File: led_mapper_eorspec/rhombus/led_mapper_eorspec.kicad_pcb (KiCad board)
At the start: 4 copper layers, 116 x 67 mm, 2117 parts, among them J1 Conn_02x12_Top_Bottom

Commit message: Complete single-net schematic, led placement and vertical tracks
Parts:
- removed D1000, D1001, D1002, D1003, D1004, D1005, D1006, D1007, D1008, D1009, D1010, D1011, D1012, D1013, D1014, D1015, D1016, D1017, D1018, D1019, D1020, D1021, D1022, D1023, D1024, D1025, D1026, D1027, D1028, D1029, D1030, D1031, D1032, D1033, D1034, D1035, D1036, D1037, D1038, D1039, D1040, D1041, D1042, D1043, D1044, D1045, D1046, D1047, D1048, D1049, D1050, D1051, D1052, D1053, D1054, D1055, D1056, D1057, D1058, D1059, D1060, D1061, D1062, D1063, D1064, D1065, D1066, D1067, D1068, D1069, D1070, D1071, D1072, D1073, D1074, D1075, D1076, D1077, D1078, D1079, D1080, D1081, D1082, D1083, D1084, D1085, D1086, D1087, D1088, D1089, D1090, D1091, D1092, D1093, D1094, D1095, D1096, D1097, D1098, D1099, D1100, D1101, D1102, D1103, D1104, D1105, D1106, D1107, D1108, D1109, D1110, D1111, D1112, D1113, D1114, D1115, D1116, D1117, D1118, D1119, D1120, D1121, D1122, D1123, D1124, D1125, D1126, D1127, D1128, D1129, D1130, D1131, D1132, D1133, D1134, D1135, D1136, D1137, D1138, D1139, D1140, D1141, D1142, D1143, D1144, D1145, D1146, D1147, D1148, D1149, D1150, D1151, D1152, D1153, D1154, D1155, D1156, D1157, D1158, D1159, D1160, D1161, D1162, D1163, D1164, D1165, D1166, D1167, D1168, D1169, D1170, D1171, D1172, D1173, D1174, D1175, D1176, D1177, D1178, D1179, D1180, D1181, D1182, D1183, D1184, D1185, D1186, D1187, D1188, D1189, D1190, D1191, D1192, D1193, D1194, D1195, D1196, D1197, D1198, D1199, D1200, D1201, D1202, D1203, D1204, D1205, D1206, D1207, D1208, D1209, D1210, D1211, D1212, D1213, D1214, D1215, D1216, D1217, D1218, D1219, D1220, D1221, D1222, D1223, D1224, D1225, D1226, D1227, D1228, D1229, D1230, D1231, D1232, D1233, D1234, D1235, D1236, D1237, D1238, D1239, D1240, D1241, D1242, D1243, D1244, D1245, D1246, D1247, D1248, D1249, D1250, D1251, D1252, D1253, D1254, D1255, D1256, D1257, D1258, D1259, D1260, D1261, D1262, D1263, D1264, D1265, D1266, D1267, D1268, D1269, D1270, D1271, D1272, D1273, D1274, D1275, D1276, D1277, D1278, D1279, D1280, D1281, D1282, D1283, D1284, D1285, D1286, D1287, D1288, D1289, D1290, D1291, D1292, D1293, D1294, D1295, D1296, D1297, D1298, D1299, D1300, D1301, D1302, D1303, D1304, D1305, D1306, D1307, D1308, D1309, D1310, D1311, D1312, D1313, D1314, D1315, D1316, D1317, D1318, D1319, D1320, D1321, D1322, D1323, D1324, D1325, D1326, D1327, D1328, D1329, D1330, D1331, D1332, D1333, D1334, D1335, D1336, D1337, D1338, D1339, D1340, D1341, D1342, D1343, D1344, D1345, D1346, D1347, D1348, D1349, D1350, D1351, D1352, D1353, D1354, D1355, D1356, D1357, D1358, D1359, D1360, D1361, D1362, D1363, D1364, D1365, D1366, D1367, D1368, D1369, D1370, D1371, D1372, D1373, D1374, D1375, D1376, D1377, D1378, D1379, D1380, D1381, D1382, D1383, D1384, D1385, D1386, D1387, D1388, D1389, D1390, D1391, D1392, D1393, D1394, D1395, D1396, D1397, D1398, D1399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: LED, ccatlib:LED_0201_0603Metric_XINGLIGHT
- D1, D10, D100, D101, D102, D103, D104, D105, D106, D107, D108, D109, D11, D110, D111, D112, D113, D114, D115, D116, D117, D118, D119, D12, D120, D121, D122, D123, D124, D125, D126, D127, D128, D129, D13, D130, D131, D132, D133, D134, D135, D136, D137, D138, D139, D14, D140, D141, D142, D143, D144, D145, D146, D147, D148, D149, D15, D150, D151, D152, D153, D154, D155, D156, D157, D158, D159, D16, D160, D161, D162, D163, D164, D165, D166, D167, D168, D169, D17, D170, D171, D172, D173, D174, D175, D176, D177, D178, D179, D18, D180, D181, D182, D183, D184, D185, D186, D187, D188, D189, D19, D190, D191, D192, D193, D194, D195, D196, D197, D198, D199, D2, D20, D200, D201, D202, D203, D204, D205, D206, D207, D208, D209, D21, D210, D211, D212, D213, D214, D215, D216, D217, D218, D219, D22, D220, D221, D222, D223, D224, D225, D226, D227, D228, D229, D23, D230, D231, D232, D233, D234, D235, D236, D237, D238, D239, D24, D240, D241, D242, D243, D244, D245, D246, D247, D248, D249, D25, D250, D251, D252, D253, D254, D255, D256, D257, D258, D259, D26, D260, D261, D262, D263, D264, D265, D266, D267, D268, D269, D27, D270, D271, D272, D273, D274, D275, D276, D277, D278, D279, D28, D280, D281, D282, D283, D284, D285, D286, D287, D288, D289, D29, D290, D291, D292, D293, D294, D295, D296, D297, D298, D299, D3, D30, D300, D301, D302, D303, D304, D305, D306, D307, D308, D309, D31, D310, D311, D312, D313, D314, D315, D316, D317, D318, D319, D32, D320, D321, D322, D323, D324, D325, D326, D327, D328, D329, D33, D330, D331, D332, D333, D334, D335, D336, D337, D338, D339, D34, D340, D341, D342, D343, D344, D345, D346, D347, D348, D349, D35, D350, D351, D352, D353, D354, D355, D356, D357, D358, D359, D36, D360, D361, D362, D363, D364, D365, D366, D367, D368, D369, D37, D370, D371, D372, D373, D374, D375, D376, D377, D378, D379, D38, D380, D381, D382, D383, D384, D385, D386, D387, D388, D389, D39, D390, D391, D392, D393, D394, D395, D396, D397, D398, D399, D4, D40, D400, D401, D402, D403, D404, D405, D406, D407, D408, D409, D41, D410, D411, D412, D413, D414, D415, D416, D417, D418, D419, D42, D420, D421, D422, D423, D424, D425, D426, D427, D428, D429, D43, D430, D431, D432, D433, D434, D435, D436, D437, D438, D439, D44, D440, D441, D442, D443, D444, D445, D446, D447, D448, D449, D45, D450, D451, D452, D453, D454, D455, D456, D457, D458, D459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: value LED -> LED_45deg; footprint ccatlib:LED_0201_0603Metric_XINGLIGHT -> LED_SMD:LED_0201_0603Metric
- moved J1 203.9 mm to (246.4, 90.7)
- moved D96 93.7 mm to (94.4, 22.5), turned to 180 degrees
- moved D416 93.6 mm to (83.9, 40.6), turned to 180 degrees
- moved D95 93.1 mm to (92.3, 22.5), turned to 180 degrees
- moved D415 93.0 mm to (81.8, 40.6), turned to 180 degrees
- moved D94 92.4 mm to (90.2, 22.5), turned to 180 degrees
- moved D93 91.7 mm to (88.1, 22.5), turned to 180 degrees
- moved D512 87.8 mm to (80.8, 46.0), turned to 180 degrees
- moved D192 87.3 mm to (91.2, 27.9), turned to 180 degrees
- moved D511 87.2 mm to (78.7, 46.0), turned to 180 degrees
- moved D191 86.7 mm to (89.2, 27.9), turned to 180 degrees
- moved D510 86.5 mm to (76.6, 46.0), turned to 180 degrees
- moved D190 86.0 mm to (87.1, 27.9), turned to 180 degrees
- moved D509 85.9 mm to (74.5, 46.0), turned to 180 degrees
- moved D189 85.3 mm to (85.0, 27.9), turned to 180 degrees
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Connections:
- D100 pad 1: /P22 -> /P21
- D100 pad 2: /P8 -> /P4
- D101 pad 1: /P22 -> /P21
- D101 pad 2: /P9 -> /P5
- D102 pad 1: /P22 -> /P21
- D102 pad 2: /P10 -> /P6
- D103 pad 1: /P22 -> /P21
- D103 pad 2: /P11 -> /P7
- D104 pad 1: /P22 -> /P21
- D104 pad 2: /P12 -> /P8
- D105 pad 1: /P22 -> /P21
- D105 pad 2: /P13 -> /P9
- D106 pad 1: /P22 -> /P21
- D106 pad 2: /P14 -> /P10
- D107 pad 1: /P22 -> /P21
- D107 pad 2: /P15 -> /P11
- D108 pad 1: /P22 -> /P21
- D108 pad 2: /P16 -> /P12
- D109 pad 1: /P22 -> /P21
- D109 pad 2: /P17 -> /P13
- D110 pad 1: /P22 -> /P21
- D110 pad 2: /P18 -> /P14
- D111 pad 1: /P22 -> /P21
- D111 pad 2: /P19 -> /P15
- D112 pad 1: /P22 -> /P21
- D112 pad 2: /P20 -> /P16
- D113 pad 1: /P22 -> /P21
- D113 pad 2: /P21 -> /P17
- D114 pad 1: /P22 -> /P21
- D114 pad 2: /P23 -> /P18
- D115 pad 1: /P22 -> /P21
- D115 pad 2: /P24 -> /P19
- D116 pad 1: /P10 -> /P21
- D116 pad 2: /P1 -> /P20
- D117 pad 1: /P10 -> /P21
- D117 pad 2: /P2 -> /P22
- D118 pad 1: /P10 -> /P21
- D118 pad 2: /P3 -> /P23
- D119 pad 1: /P10 -> /P21
- D119 pad 2: /P4 -> /P24
- D120 pad 1: /P10 -> /P5
- D120 pad 2: /P5 -> /P1
- D121 pad 1: /P10 -> /P5
- D121 pad 2: /P6 -> /P2
- D122 pad 1: /P10 -> /P5
- D122 pad 2: /P7 -> /P3
- D123 pad 1: /P10 -> /P5
- D123 pad 2: /P8 -> /P4
- D124 pad 1: /P10 -> /P5
- D124 pad 2: /P9 -> /P6
- D125 pad 1: /P10 -> /P5
- D125 pad 2: /P11 -> /P7
- D126 pad 1: /P10 -> /P5
- D126 pad 2: /P12 -> /P8
- D127 pad 1: /P10 -> /P5
- D127 pad 2: /P13 -> /P9
- D128 pad 1: /P10 -> /P5
- D128 pad 2: /P14 -> /P10
- D129 pad 1: /P10 -> /P20
- D129 pad 2: /P15 -> /P1
- D130 pad 1: /P10 -> /P20
- D130 pad 2: /P16 -> /P2
- D131 pad 1: /P10 -> /P20
- D131 pad 2: /P17 -> /P3
- D132 pad 1: /P10 -> /P20
- D132 pad 2: /P18 -> /P4
- D133 pad 1: /P10 -> /P20
- D133 pad 2: /P19 -> /P5
- D134 pad 1: /P10 -> /P20
- D134 pad 2: /P20 -> /P6
- D135 pad 1: /P10 -> /P20
- D135 pad 2: /P21 -> /P7
- D136 pad 1: /P10 -> /P20
- D136 pad 2: /P22 -> /P8
- D137 pad 1: /P10 -> /P20
- D137 pad 2: /P23 -> /P9
- D138 pad 1: /P10 -> /P20
- D138 pad 2: /P24 -> /P10
- D139 pad 1: /P21 -> /P20
- D139 pad 2: /P1 -> /P11
- D140 pad 1: /P21 -> /P20
- D140 pad 2: /P2 -> /P12
- D141 pad 1: /P21 -> /P20
- D141 pad 2: /P3 -> /P13
- D142 pad 1: /P21 -> /P20
- D142 pad 2: /P4 -> /P14
- D143 pad 1: /P21 -> /P20
- D143 pad 2: /P5 -> /P15
- D144 pad 1: /P21 -> /P20
- D144 pad 2: /P6 -> /P16
- D145 pad 1: /P21 -> /P20
- D145 pad 2: /P7 -> /P17
- D146 pad 1: /P21 -> /P20
- D146 pad 2: /P8 -> /P18
- D147 pad 1: /P21 -> /P20
- D147 pad 2: /P9 -> /P19
- D148 pad 1: /P21 -> /P20
- D148 pad 2: /P10 -> /P21
- D149 pad 1: /P21 -> /P20
- D149 pad 2: /P11 -> /P22
- D150 pad 1: /P21 -> /P20
- D150 pad 2: /P12 -> /P23
- D151 pad 1: /P21 -> /P20
- D151 pad 2: /P13 -> /P24
- D152 pad 1: /P21 -> /P4
- D152 pad 2: /P14 -> /P1
- D153 pad 1: /P21 -> /P4
- D153 pad 2: /P15 -> /P2
- D154 pad 1: /P21 -> /P4
- D154 pad 2: /P16 -> /P3
- D155 pad 1: /P21 -> /P4
- D155 pad 2: /P17 -> /P5
- D156 pad 1: /P21 -> /P4
- D156 pad 2: /P18 -> /P6
- D157 pad 1: /P21 -> /P4
- D157 pad 2: /P19 -> /P7
- D158 pad 1: /P21 -> /P4
- D158 pad 2: /P20 -> /P8
- D159 pad 1: /P21 -> /P4
- D159 pad 2: /P22 -> /P9
- D160 pad 1: /P21 -> /P4
- D160 pad 2: /P23 -> /P10
- D161 pad 1: /P21 -> /P19
- D161 pad 2: /P24 -> /P1
- D162 pad 1: /P9 -> /P19
- D162 pad 2: /P1 -> /P2
- D163 pad 1: /P9 -> /P19
- D163 pad 2: /P2 -> /P3
- D164 pad 1: /P9 -> /P19
- D164 pad 2: /P3 -> /P4
- D165 pad 1: /P9 -> /P19
- D165 pad 2: /P4 -> /P5
- D166 pad 1: /P9 -> /P19
- D166 pad 2: /P5 -> /P6
- D167 pad 1: /P9 -> /P19
- D167 pad 2: /P6 -> /P7
- D168 pad 1: /P9 -> /P19
- D168 pad 2: /P7 -> /P8
- D169 pad 1: /P9 -> /P19
- D169 pad 2: /P8 -> /P9
- D170 pad 1: /P9 -> /P19
- D171 pad 1: /P9 -> /P19
- D172 pad 1: /P9 -> /P19
- D173 pad 1: /P9 -> /P19
- D174 pad 1: /P9 -> /P19
- D175 pad 1: /P9 -> /P19
- D176 pad 1: /P9 -> /P19
- D177 pad 1: /P9 -> /P19
- D178 pad 1: /P9 -> /P19
- D179 pad 1: /P9 -> /P19
- D179 pad 2: /P19 -> /P20
- D180 pad 1: /P9 -> /P19
- D180 pad 2: /P20 -> /P21
- D181 pad 1: /P9 -> /P19
- D181 pad 2: /P21 -> /P22
- D182 pad 1: /P9 -> /P19
- D182 pad 2: /P22 -> /P23
- D183 pad 1: /P9 -> /P19
- D183 pad 2: /P23 -> /P24
- D184 pad 1: /P9 -> /P3
- D184 pad 2: /P24 -> /P1
- D185 pad 1: /P20 -> /P3
- D185 pad 2: /P1 -> /P2
- D186 pad 1: /P20 -> /P3
- D186 pad 2: /P2 -> /P4
- D187 pad 1: /P20 -> /P3
- D187 pad 2: /P3 -> /P5
- D188 pad 1: /P20 -> /P3
- D188 pad 2: /P4 -> /P6
- D189 pad 1: /P20 -> /P3
- D189 pad 2: /P5 -> /P7
- D190 pad 1: /P20 -> /P3
- D190 pad 2: /P6 -> /P8
- D191 pad 1: /P20 -> /P3
- D191 pad 2: /P7 -> /P9
- D192 pad 1: /P20 -> /P3
- D192 pad 2: /P8 -> /P10
- D193 pad 1: /P20 -> /P18
- D193 pad 2: /P9 -> /P1
- D194 pad 1: /P20 -> /P18
- D194 pad 2: /P10 -> /P2
- D195 pad 1: /P20 -> /P18
- D195 pad 2: /P11 -> /P3
- D196 pad 1: /P20 -> /P18
- D196 pad 2: /P12 -> /P4
- D197 pad 1: /P20 -> /P18
- D197 pad 2: /P13 -> /P5
- D198 pad 1: /P20 -> /P18
- D198 pad 2: /P14 -> /P6
- D199 pad 1: /P20 -> /P18
- D199 pad 2: /P15 -> /P7
- D200 pad 1: /P20 -> /P18
- D200 pad 2: /P16 -> /P8
- D201 pad 1: /P20 -> /P18
- D201 pad 2: /P17 -> /P9
- D202 pad 1: /P20 -> /P18
- D202 pad 2: /P18 -> /P10
- D203 pad 1: /P20 -> /P18
- D203 pad 2: /P19 -> /P11
- D204 pad 1: /P20 -> /P18
- D204 pad 2: /P21 -> /P12
- D205 pad 1: /P20 -> /P18
- D205 pad 2: /P22 -> /P13
- D206 pad 1: /P20 -> /P18
- D206 pad 2: /P23 -> /P14
- D207 pad 1: /P20 -> /P18
- D207 pad 2: /P24 -> /P15
- D208 pad 1: /P8 -> /P18
- D208 pad 2: /P1 -> /P16
- D209 pad 1: /P8 -> /P18
- D209 pad 2: /P2 -> /P17
- D210 pad 1: /P8 -> /P18
- D210 pad 2: /P3 -> /P19
- D211 pad 1: /P8 -> /P18
- D211 pad 2: /P4 -> /P20
- D212 pad 1: /P8 -> /P18
- D212 pad 2: /P5 -> /P21
- D213 pad 1: /P8 -> /P18
- D213 pad 2: /P6 -> /P22
- D214 pad 1: /P8 -> /P18
- D214 pad 2: /P7 -> /P23
- D215 pad 1: /P8 -> /P18
- D215 pad 2: /P9 -> /P24
- D216 pad 1: /P8 -> /P2
- D216 pad 2: /P10 -> /P1
- D217 pad 1: /P8 -> /P2
- D217 pad 2: /P11 -> /P3
- D218 pad 1: /P8 -> /P2
- D218 pad 2: /P12 -> /P4
- D219 pad 1: /P8 -> /P2
- D219 pad 2: /P13 -> /P5
- D220 pad 1: /P8 -> /P2
- D220 pad 2: /P14 -> /P6
- D221 pad 1: /P8 -> /P2
- D221 pad 2: /P15 -> /P7
- D222 pad 1: /P8 -> /P2
- D222 pad 2: /P16 -> /P8
- D223 pad 1: /P8 -> /P2
- D223 pad 2: /P17 -> /P9
- D224 pad 1: /P8 -> /P2
- D224 pad 2: /P18 -> /P10
- D225 pad 1: /P8 -> /P17
- D225 pad 2: /P19 -> /P1
- D226 pad 1: /P8 -> /P17
- D226 pad 2: /P20 -> /P2
- D227 pad 1: /P8 -> /P17
- D227 pad 2: /P21 -> /P3
- D228 pad 1: /P8 -> /P17
- D228 pad 2: /P22 -> /P4
- D229 pad 1: /P8 -> /P17
- D229 pad 2: /P23 -> /P5
- D230 pad 1: /P8 -> /P17
- D230 pad 2: /P24 -> /P6
- D231 pad 1: /P19 -> /P17
- D231 pad 2: /P1 -> /P7
- D232 pad 1: /P19 -> /P17
- D232 pad 2: /P2 -> /P8
- D233 pad 1: /P19 -> /P17
- D233 pad 2: /P3 -> /P9
- D234 pad 1: /P19 -> /P17
- D234 pad 2: /P4 -> /P10
- D235 pad 1: /P19 -> /P17
- D235 pad 2: /P5 -> /P11
- D236 pad 1: /P19 -> /P17
- D236 pad 2: /P6 -> /P12
- D237 pad 1: /P19 -> /P17
- D237 pad 2: /P7 -> /P13
- D238 pad 1: /P19 -> /P17
- D238 pad 2: /P8 -> /P14
- D239 pad 1: /P19 -> /P17
- D239 pad 2: /P9 -> /P15
- D24 pad 1: /P12 -> /P8
- D240 pad 1: /P19 -> /P17
- D240 pad 2: /P10 -> /P16
- D241 pad 1: /P19 -> /P17
- D241 pad 2: /P11 -> /P18
- D242 pad 1: /P19 -> /P17
- D242 pad 2: /P12 -> /P19
- D243 pad 1: /P19 -> /P17
- D243 pad 2: /P13 -> /P20
- D244 pad 1: /P19 -> /P17
- D244 pad 2: /P14 -> /P21
- D245 pad 1: /P19 -> /P17
- D245 pad 2: /P15 -> /P22
- D246 pad 1: /P19 -> /P17
- D246 pad 2: /P16 -> /P23
- D247 pad 1: /P19 -> /P17
- D247 pad 2: /P17 -> /P24
- D248 pad 1: /P19 -> /P1
- D248 pad 2: /P18 -> /P2
- D249 pad 1: /P19 -> /P1
- D249 pad 2: /P20 -> /P3
- D25 pad 1: /P12 -> /P8
- D250 pad 1: /P19 -> /P1
- D250 pad 2: /P21 -> /P4
- D251 pad 1: /P19 -> /P1
- D251 pad 2: /P22 -> /P5
- D252 pad 1: /P19 -> /P1
- D252 pad 2: /P23 -> /P6
- D253 pad 1: /P19 -> /P1
- D253 pad 2: /P24 -> /P7
- D254 pad 1: /P7 -> /P1
- D254 pad 2: /P1 -> /P8
- D255 pad 1: /P7 -> /P1
- D255 pad 2: /P2 -> /P9
- D256 pad 1: /P7 -> /P1
- D256 pad 2: /P3 -> /P10
- D257 pad 1: /P7 -> /P16
- D257 pad 2: /P4 -> /P1
- D258 pad 1: /P7 -> /P16
- D258 pad 2: /P5 -> /P2
- D259 pad 1: /P7 -> /P16
- D259 pad 2: /P6 -> /P3
- D26 pad 1: /P12 -> /P8
- D260 pad 1: /P7 -> /P16
- D260 pad 2: /P8 -> /P4
- D261 pad 1: /P7 -> /P16
- D261 pad 2: /P9 -> /P5
- D262 pad 1: /P7 -> /P16
- D262 pad 2: /P10 -> /P6
- D263 pad 1: /P7 -> /P16
- D263 pad 2: /P11 -> /P7
- D264 pad 1: /P7 -> /P16
- D264 pad 2: /P12 -> /P8
- D265 pad 1: /P7 -> /P16
- D265 pad 2: /P13 -> /P9
- D266 pad 1: /P7 -> /P16
- D266 pad 2: /P14 -> /P10
- D267 pad 1: /P7 -> /P16
- D267 pad 2: /P15 -> /P11
- D268 pad 1: /P7 -> /P16
- D268 pad 2: /P16 -> /P12
- D269 pad 1: /P7 -> /P16
- D269 pad 2: /P17 -> /P13
- D27 pad 1: /P12 -> /P8
- D270 pad 1: /P7 -> /P16
- D270 pad 2: /P18 -> /P14
- D271 pad 1: /P7 -> /P16
- D271 pad 2: /P19 -> /P15
- D272 pad 1: /P7 -> /P16
- D272 pad 2: /P20 -> /P17
- D273 pad 1: /P7 -> /P16
- D273 pad 2: /P21 -> /P18
- D274 pad 1: /P7 -> /P16
- D274 pad 2: /P22 -> /P19
- D275 pad 1: /P7 -> /P16
- D275 pad 2: /P23 -> /P20
- D276 pad 1: /P7 -> /P16
- D276 pad 2: /P24 -> /P21
- D277 pad 1: /P18 -> /P16
- D277 pad 2: /P1 -> /P22
- D278 pad 1: /P18 -> /P16
- D278 pad 2: /P2 -> /P23
- D279 pad 1: /P18 -> /P16
- D279 pad 2: /P3 -> /P24
- D28 pad 1: /P12 -> /P8
- D280 pad 1: /P18 -> /P8
- D280 pad 2: /P4 -> /P11
- D281 pad 1: /P18 -> /P8
- D281 pad 2: /P5 -> /P12
- D282 pad 1: /P18 -> /P8
- D282 pad 2: /P6 -> /P13
- D283 pad 1: /P18 -> /P8
- D283 pad 2: /P7 -> /P14
- D284 pad 1: /P18 -> /P8
- D284 pad 2: /P8 -> /P15
- D285 pad 1: /P18 -> /P8
- D285 pad 2: /P9 -> /P16
- D286 pad 1: /P18 -> /P8
- D286 pad 2: /P10 -> /P17
- D287 pad 1: /P18 -> /P8
- D287 pad 2: /P11 -> /P18
- D288 pad 1: /P18 -> /P8
- D288 pad 2: /P12 -> /P19
- D289 pad 1: /P18 -> /P15
- D289 pad 2: /P13 -> /P1
- D29 pad 1: /P12 -> /P8
- D290 pad 1: /P18 -> /P15
- D290 pad 2: /P14 -> /P2
- D291 pad 1: /P18 -> /P15
- D291 pad 2: /P15 -> /P3
- D292 pad 1: /P18 -> /P15
- D292 pad 2: /P16 -> /P4
- D293 pad 1: /P18 -> /P15
- D293 pad 2: /P17 -> /P5
- D294 pad 1: /P18 -> /P15
- D294 pad 2: /P19 -> /P6
- D295 pad 1: /P18 -> /P15
- D295 pad 2: /P20 -> /P7
- D296 pad 1: /P18 -> /P15
- D296 pad 2: /P21 -> /P8
- D297 pad 1: /P18 -> /P15
- D297 pad 2: /P22 -> /P9
- D298 pad 1: /P18 -> /P15
- D298 pad 2: /P23 -> /P10
- D299 pad 1: /P18 -> /P15
- D299 pad 2: /P24 -> /P11
- D30 pad 1: /P12 -> /P8
- D300 pad 1: /P6 -> /P15
- D300 pad 2: /P1 -> /P12
- D301 pad 1: /P6 -> /P15
- D301 pad 2: /P2 -> /P13
- D302 pad 1: /P6 -> /P15
- D302 pad 2: /P3 -> /P14
- D303 pad 1: /P6 -> /P15
- D303 pad 2: /P4 -> /P16
- D304 pad 1: /P6 -> /P15
- D304 pad 2: /P5 -> /P17
- D305 pad 1: /P6 -> /P15
- D305 pad 2: /P7 -> /P18
- D306 pad 1: /P6 -> /P15
- D306 pad 2: /P8 -> /P19
- D307 pad 1: /P6 -> /P15
- D307 pad 2: /P9 -> /P20
- D308 pad 1: /P6 -> /P15
- D308 pad 2: /P10 -> /P21
- D309 pad 1: /P6 -> /P15
- D309 pad 2: /P11 -> /P22
- D31 pad 1: /P12 -> /P8
- D31 pad 2: /P8 -> /P9
- D310 pad 1: /P6 -> /P15
- D310 pad 2: /P12 -> /P23
- D311 pad 1: /P6 -> /P15
- D311 pad 2: /P13 -> /P24
- D312 pad 1: /P6 -> /P7
- D312 pad 2: /P14 -> /P11
- D313 pad 1: /P6 -> /P7
- D313 pad 2: /P15 -> /P12
- D314 pad 1: /P6 -> /P7
- D314 pad 2: /P16 -> /P13
- D315 pad 1: /P6 -> /P7
- D315 pad 2: /P17 -> /P14
- D316 pad 1: /P6 -> /P7
- D316 pad 2: /P18 -> /P15
- D317 pad 1: /P6 -> /P7
- D317 pad 2: /P19 -> /P16
- D318 pad 1: /P6 -> /P7
- D318 pad 2: /P20 -> /P17
- D319 pad 1: /P6 -> /P7
- D319 pad 2: /P21 -> /P18
- D32 pad 1: /P12 -> /P8
- D32 pad 2: /P9 -> /P10
- D320 pad 1: /P6 -> /P7
- D320 pad 2: /P22 -> /P19
- D321 pad 1: /P6 -> /P14
- D321 pad 2: /P23 -> /P1
- D322 pad 1: /P6 -> /P14
- D322 pad 2: /P24 -> /P2
- D323 pad 1: /P17 -> /P14
- D323 pad 2: /P1 -> /P3
- D324 pad 1: /P17 -> /P14
- D324 pad 2: /P2 -> /P4
- D325 pad 1: /P17 -> /P14
- D325 pad 2: /P3 -> /P5
- D326 pad 1: /P17 -> /P14
- D326 pad 2: /P4 -> /P6
- D327 pad 1: /P17 -> /P14
- D327 pad 2: /P5 -> /P7
- D328 pad 1: /P17 -> /P14
- D328 pad 2: /P6 -> /P8
- D329 pad 1: /P17 -> /P14
- D329 pad 2: /P7 -> /P9
- D33 pad 1: /P12 -> /P23
- D33 pad 2: /P10 -> /P1
- D330 pad 1: /P17 -> /P14
- D330 pad 2: /P8 -> /P10
- D331 pad 1: /P17 -> /P14
- D331 pad 2: /P9 -> /P11
- D332 pad 1: /P17 -> /P14
- D332 pad 2: /P10 -> /P12
- D333 pad 1: /P17 -> /P14
- D333 pad 2: /P11 -> /P13
- D334 pad 1: /P17 -> /P14
- D334 pad 2: /P12 -> /P15
- D335 pad 1: /P17 -> /P14
- D335 pad 2: /P13 -> /P16
- D336 pad 1: /P17 -> /P14
- D336 pad 2: /P14 -> /P17
- D337 pad 1: /P17 -> /P14
- D337 pad 2: /P15 -> /P18
- D338 pad 1: /P17 -> /P14
- D338 pad 2: /P16 -> /P19
- D339 pad 1: /P17 -> /P14
- D339 pad 2: /P18 -> /P20
- D34 pad 1: /P12 -> /P23
- D34 pad 2: /P11 -> /P2
- D340 pad 1: /P17 -> /P14
- D340 pad 2: /P19 -> /P21
- D341 pad 1: /P17 -> /P14
- D341 pad 2: /P20 -> /P22
- D342 pad 1: /P17 -> /P14
- D342 pad 2: /P21 -> /P23
- D343 pad 1: /P17 -> /P14
- D343 pad 2: /P22 -> /P24
- D344 pad 1: /P17 -> /P6
- D344 pad 2: /P23 -> /P11
- D345 pad 1: /P17 -> /P6
- D345 pad 2: /P24 -> /P12
- D346 pad 1: /P5 -> /P6
- D346 pad 2: /P1 -> /P13
- D347 pad 1: /P5 -> /P6
- D347 pad 2: /P2 -> /P14
- D348 pad 1: /P5 -> /P6
- D348 pad 2: /P3 -> /P15
- D349 pad 1: /P5 -> /P6
- D349 pad 2: /P4 -> /P16
- D35 pad 1: /P12 -> /P23
- D35 pad 2: /P13 -> /P3
- D350 pad 1: /P5 -> /P6
- D350 pad 2: /P6 -> /P17
- D351 pad 1: /P5 -> /P6
- D351 pad 2: /P7 -> /P18
- D352 pad 1: /P5 -> /P6
- D352 pad 2: /P8 -> /P19
- D353 pad 1: /P5 -> /P13
- D353 pad 2: /P9 -> /P1
- D354 pad 1: /P5 -> /P13
- D354 pad 2: /P10 -> /P2
- D355 pad 1: /P5 -> /P13
- D355 pad 2: /P11 -> /P3
- D356 pad 1: /P5 -> /P13
- D356 pad 2: /P12 -> /P4
- D357 pad 1: /P5 -> /P13
- D357 pad 2: /P13 -> /P5
- D358 pad 1: /P5 -> /P13
- D358 pad 2: /P14 -> /P6
- D359 pad 1: /P5 -> /P13
- D359 pad 2: /P15 -> /P7
- D36 pad 1: /P12 -> /P23
- D36 pad 2: /P14 -> /P4
- D360 pad 1: /P5 -> /P13
- D360 pad 2: /P16 -> /P8
- D361 pad 1: /P5 -> /P13
- D361 pad 2: /P17 -> /P9
- D362 pad 1: /P5 -> /P13
- D362 pad 2: /P18 -> /P10
- D363 pad 1: /P5 -> /P13
- D363 pad 2: /P19 -> /P11
- D364 pad 1: /P5 -> /P13
- D364 pad 2: /P20 -> /P12
- D365 pad 1: /P5 -> /P13
- D365 pad 2: /P21 -> /P14
- D366 pad 1: /P5 -> /P13
- D366 pad 2: /P22 -> /P15
- D367 pad 1: /P5 -> /P13
- D367 pad 2: /P23 -> /P16
- D368 pad 1: /P5 -> /P13
- D368 pad 2: /P24 -> /P17
- D369 pad 1: /P16 -> /P13
- D369 pad 2: /P1 -> /P18
- D37 pad 1: /P12 -> /P23
- D37 pad 2: /P15 -> /P5
- D370 pad 1: /P16 -> /P13
- D370 pad 2: /P2 -> /P19
- D371 pad 1: /P16 -> /P13
- D371 pad 2: /P3 -> /P20
- D372 pad 1: /P16 -> /P13
- D372 pad 2: /P4 -> /P21
- D373 pad 1: /P16 -> /P13
- D373 pad 2: /P5 -> /P22
- D374 pad 1: /P16 -> /P13
- D374 pad 2: /P6 -> /P23
- D375 pad 1: /P16 -> /P13
- D375 pad 2: /P7 -> /P24
- D376 pad 1: /P16 -> /P5
- D376 pad 2: /P8 -> /P11
- D377 pad 1: /P16 -> /P5
- D377 pad 2: /P9 -> /P12
- D378 pad 1: /P16 -> /P5
- D378 pad 2: /P10 -> /P13
- D379 pad 1: /P16 -> /P5
- D379 pad 2: /P11 -> /P14
- D38 pad 1: /P12 -> /P23
- D38 pad 2: /P16 -> /P6
- D380 pad 1: /P16 -> /P5
- D380 pad 2: /P12 -> /P15
- D381 pad 1: /P16 -> /P5
- D381 pad 2: /P13 -> /P16
- D382 pad 1: /P16 -> /P5
- D382 pad 2: /P14 -> /P17
- D383 pad 1: /P16 -> /P5
- D383 pad 2: /P15 -> /P18
- D384 pad 1: /P16 -> /P5
- D384 pad 2: /P17 -> /P19
- D385 pad 1: /P16 -> /P12
- D385 pad 2: /P18 -> /P1
- D386 pad 1: /P16 -> /P12
- D386 pad 2: /P19 -> /P2
- D387 pad 1: /P16 -> /P12
- D387 pad 2: /P20 -> /P3
- D388 pad 1: /P16 -> /P12
- D388 pad 2: /P21 -> /P4
- D389 pad 1: /P16 -> /P12
- D389 pad 2: /P22 -> /P5
- D39 pad 1: /P12 -> /P23
- D39 pad 2: /P17 -> /P7
- D390 pad 1: /P16 -> /P12
- D390 pad 2: /P23 -> /P6
- D391 pad 1: /P16 -> /P12
- D391 pad 2: /P24 -> /P7
- D392 pad 1: /P4 -> /P12
- D392 pad 2: /P1 -> /P8
- D393 pad 1: /P4 -> /P12
- D393 pad 2: /P2 -> /P9
- D394 pad 1: /P4 -> /P12
- D394 pad 2: /P3 -> /P10
- D395 pad 1: /P4 -> /P12
- D395 pad 2: /P5 -> /P11
- D396 pad 1: /P4 -> /P12
- D396 pad 2: /P6 -> /P13
- D397 pad 1: /P4 -> /P12
- D397 pad 2: /P7 -> /P14
- D398 pad 1: /P4 -> /P12
- D398 pad 2: /P8 -> /P15
- D399 pad 1: /P4 -> /P12
- D399 pad 2: /P9 -> /P16
- D40 pad 1: /P12 -> /P23
- D40 pad 2: /P18 -> /P8
- D400 pad 1: /P4 -> /P12
- D400 pad 2: /P10 -> /P17
- D401 pad 1: /P4 -> /P12
- D401 pad 2: /P11 -> /P18
- D402 pad 1: /P4 -> /P12
- D402 pad 2: /P12 -> /P19
- D403 pad 1: /P4 -> /P12
- D403 pad 2: /P13 -> /P20
- D404 pad 1: /P4 -> /P12
- D404 pad 2: /P14 -> /P21
- D405 pad 1: /P4 -> /P12
- D405 pad 2: /P15 -> /P22
- D406 pad 1: /P4 -> /P12
- D406 pad 2: /P16 -> /P23
- D407 pad 1: /P4 -> /P12
- D407 pad 2: /P17 -> /P24
- D408 pad 2: /P18 -> /P11
- D409 pad 2: /P19 -> /P12
- D41 pad 1: /P12 -> /P23
- D41 pad 2: /P19 -> /P9
- D410 pad 2: /P20 -> /P13
- D411 pad 2: /P21 -> /P14
- D412 pad 2: /P22 -> /P15
- D413 pad 2: /P23 -> /P16
- D414 pad 2: /P24 -> /P17
- D415 pad 1: /P15 -> /P4
- D415 pad 2: /P1 -> /P18
- D416 pad 1: /P15 -> /P4
- D416 pad 2: /P2 -> /P19
- D417 pad 1: /P15 -> /P11
- D417 pad 2: /P3 -> /P1
- D418 pad 1: /P15 -> /P11
- D418 pad 2: /P4 -> /P2
- D419 pad 1: /P15 -> /P11
- D419 pad 2: /P5 -> /P3
- D42 pad 1: /P12 -> /P23
- D42 pad 2: /P20 -> /P10
- D420 pad 1: /P15 -> /P11
- D420 pad 2: /P6 -> /P4
- D421 pad 1: /P15 -> /P11
- D421 pad 2: /P7 -> /P5
- D422 pad 1: /P15 -> /P11
- D422 pad 2: /P8 -> /P6
- D423 pad 1: /P15 -> /P11
- D423 pad 2: /P9 -> /P7
- D424 pad 1: /P15 -> /P11
- D424 pad 2: /P10 -> /P8
- D425 pad 1: /P15 -> /P11
- D425 pad 2: /P11 -> /P9
- D426 pad 1: /P15 -> /P11
- D426 pad 2: /P12 -> /P10
- D427 pad 1: /P15 -> /P11
- D427 pad 2: /P13 -> /P12
- D428 pad 1: /P15 -> /P11
- D428 pad 2: /P14 -> /P13
- D429 pad 1: /P15 -> /P11
- D429 pad 2: /P16 -> /P14
- D43 pad 1: /P12 -> /P23
- D43 pad 2: /P21 -> /P11
- D430 pad 1: /P15 -> /P11
- D430 pad 2: /P17 -> /P15
- D431 pad 1: /P15 -> /P11
- D431 pad 2: /P18 -> /P16
- D432 pad 1: /P15 -> /P11
- D432 pad 2: /P19 -> /P17
- D433 pad 1: /P15 -> /P11
- D433 pad 2: /P20 -> /P18
- D434 pad 1: /P15 -> /P11
- D434 pad 2: /P21 -> /P19
- D435 pad 1: /P15 -> /P11
- D435 pad 2: /P22 -> /P20
- D436 pad 1: /P15 -> /P11
- D436 pad 2: /P23 -> /P21
- D437 pad 1: /P15 -> /P11
- D437 pad 2: /P24 -> /P22
- D438 pad 1: /P3 -> /P11
- D438 pad 2: /P1 -> /P23
- D439 pad 1: /P3 -> /P11
- D439 pad 2: /P2 -> /P24
- D44 pad 1: /P12 -> /P23
- D44 pad 2: /P22 -> /P12
- D440 pad 2: /P4 -> /P11
- D441 pad 2: /P5 -> /P12
- D442 pad 2: /P6 -> /P13
- D443 pad 2: /P7 -> /P14
- D444 pad 2: /P8 -> /P15
- D445 pad 2: /P9 -> /P16
- D446 pad 2: /P10 -> /P17
- D447 pad 2: /P11 -> /P18
- D448 pad 2: /P12 -> /P19
- D449 pad 1: /P3 -> /P10
- D449 pad 2: /P13 -> /P1
- D45 pad 1: /P12 -> /P23
- D45 pad 2: /P23 -> /P13
- D450 pad 1: /P3 -> /P10
- D450 pad 2: /P14 -> /P2
- D451 pad 1: /P3 -> /P10
- D451 pad 2: /P15 -> /P3
- D452 pad 1: /P3 -> /P10
- D452 pad 2: /P16 -> /P4
- D453 pad 1: /P3 -> /P10
- D453 pad 2: /P17 -> /P5
- D454 pad 1: /P3 -> /P10
- D454 pad 2: /P18 -> /P6
- D455 pad 1: /P3 -> /P10
- D455 pad 2: /P19 -> /P7
- D456 pad 1: /P3 -> /P10
- D456 pad 2: /P20 -> /P8
- D457 pad 1: /P3 -> /P10
- D457 pad 2: /P21 -> /P9
- D458 pad 1: /P3 -> /P10
- D458 pad 2: /P22 -> /P11
- D459 pad 1: /P3 -> /P10
- D459 pad 2: /P23 -> /P12
- D46 pad 1: /P12 -> /P23
- D46 pad 2: /P24 -> /P14
- D460 pad 1: /P3 -> /P10
- D460 pad 2: /P24 -> /P13
- D461 pad 1: /P14 -> /P10
- D461 pad 2: /P1 -> /P14
- D462 pad 1: /P14 -> /P10
- D462 pad 2: /P2 -> /P15
- D463 pad 1: /P14 -> /P10
- D463 pad 2: /P3 -> /P16
- D464 pad 1: /P14 -> /P10
- D464 pad 2: /P4 -> /P17
- D465 pad 1: /P14 -> /P10
- D465 pad 2: /P5 -> /P18
- D466 pad 1: /P14 -> /P10
- D466 pad 2: /P6 -> /P19
- D467 pad 1: /P14 -> /P10
- D467 pad 2: /P7 -> /P20
- D468 pad 1: /P14 -> /P10
- D468 pad 2: /P8 -> /P21
- D469 pad 1: /P14 -> /P10
- D469 pad 2: /P9 -> /P22
- D47 pad 2: /P1 -> /P15
- D470 pad 1: /P14 -> /P10
- D470 pad 2: /P10 -> /P23
- D471 pad 1: /P14 -> /P10
- D471 pad 2: /P11 -> /P24
- D472 pad 1: /P14 -> /P2
- D472 pad 2: /P12 -> /P11
- D473 pad 1: /P14 -> /P2
- D473 pad 2: /P13 -> /P12
- D474 pad 1: /P14 -> /P2
- D474 pad 2: /P15 -> /P13
- D475 pad 1: /P14 -> /P2
- D475 pad 2: /P16 -> /P14
- D476 pad 1: /P14 -> /P2
- D476 pad 2: /P17 -> /P15
- D477 pad 1: /P14 -> /P2
- D477 pad 2: /P18 -> /P16
- D478 pad 1: /P14 -> /P2
- D478 pad 2: /P19 -> /P17
- D479 pad 1: /P14 -> /P2
- D479 pad 2: /P20 -> /P18
- D48 pad 2: /P2 -> /P16
- D480 pad 1: /P14 -> /P2
- D480 pad 2: /P21 -> /P19
- D481 pad 1: /P14 -> /P9
- D481 pad 2: /P22 -> /P1
- D482 pad 1: /P14 -> /P9
- D482 pad 2: /P23 -> /P2
- D483 pad 1: /P14 -> /P9
- D483 pad 2: /P24 -> /P3
- D484 pad 1: /P2 -> /P9
- D484 pad 2: /P1 -> /P4
- D485 pad 1: /P2 -> /P9
- D485 pad 2: /P3 -> /P5
- D486 pad 1: /P2 -> /P9
- D486 pad 2: /P4 -> /P6
- D487 pad 1: /P2 -> /P9
- D487 pad 2: /P5 -> /P7
- D488 pad 1: /P2 -> /P9
- D488 pad 2: /P6 -> /P8
- D489 pad 1: /P2 -> /P9
- D489 pad 2: /P7 -> /P10
- D49 pad 2: /P3 -> /P17
- D490 pad 1: /P2 -> /P9
- D490 pad 2: /P8 -> /P11
- D491 pad 1: /P2 -> /P9
- D491 pad 2: /P9 -> /P12
- D492 pad 1: /P2 -> /P9
- D492 pad 2: /P10 -> /P13
- D493 pad 1: /P2 -> /P9
- D493 pad 2: /P11 -> /P14
- D494 pad 1: /P2 -> /P9
- D494 pad 2: /P12 -> /P15
- D495 pad 1: /P2 -> /P9
- D495 pad 2: /P13 -> /P16
- D496 pad 1: /P2 -> /P9
- D496 pad 2: /P14 -> /P17
- D497 pad 1: /P2 -> /P9
- D497 pad 2: /P15 -> /P18
- D498 pad 1: /P2 -> /P9
- D498 pad 2: /P16 -> /P19
- D499 pad 1: /P2 -> /P9
- D499 pad 2: /P17 -> /P20
- D50 pad 2: /P4 -> /P18
- D500 pad 1: /P2 -> /P9
- D500 pad 2: /P18 -> /P21
- D501 pad 1: /P2 -> /P9
- D501 pad 2: /P19 -> /P22
- D502 pad 1: /P2 -> /P9
- D502 pad 2: /P20 -> /P23
- D503 pad 1: /P2 -> /P9
- D503 pad 2: /P21 -> /P24
- D504 pad 1: /P2 -> /P1
- D504 pad 2: /P22 -> /P11
- D505 pad 1: /P2 -> /P1
- D505 pad 2: /P23 -> /P12
- D506 pad 1: /P2 -> /P1
- D506 pad 2: /P24 -> /P13
- D507 pad 1: /P13 -> /P1
- D507 pad 2: /P1 -> /P14
- D508 pad 1: /P13 -> /P1
- D508 pad 2: /P2 -> /P15
- D509 pad 1: /P13 -> /P1
- D509 pad 2: /P3 -> /P16
- D51 pad 2: /P5 -> /P19
- D510 pad 1: /P13 -> /P1
- D510 pad 2: /P4 -> /P17
- D511 pad 1: /P13 -> /P1
- D511 pad 2: /P5 -> /P18
- D512 pad 1: /P13 -> /P1
- D512 pad 2: /P6 -> /P19
- D52 pad 2: /P6 -> /P20
- D53 pad 2: /P7 -> /P21
- D54 pad 2: /P8 -> /P22
- D55 pad 2: /P9 -> /P24
- D56 pad 1: /P23 -> /P7
- D56 pad 2: /P10 -> /P1
- D57 pad 1: /P23 -> /P7
- D57 pad 2: /P11 -> /P2
- D58 pad 1: /P23 -> /P7
- D58 pad 2: /P12 -> /P3
- D59 pad 1: /P23 -> /P7
- D59 pad 2: /P13 -> /P4
- D60 pad 1: /P23 -> /P7
- D60 pad 2: /P14 -> /P5
- D61 pad 1: /P23 -> /P7
- D61 pad 2: /P15 -> /P6
- D62 pad 1: /P23 -> /P7
- D62 pad 2: /P16 -> /P8
- D63 pad 1: /P23 -> /P7
- D63 pad 2: /P17 -> /P9
- D64 pad 1: /P23 -> /P7
- D64 pad 2: /P18 -> /P10
- D65 pad 1: /P23 -> /P22
- D65 pad 2: /P19 -> /P1
- D66 pad 1: /P23 -> /P22
- D66 pad 2: /P20 -> /P2
- D67 pad 1: /P23 -> /P22
- D67 pad 2: /P21 -> /P3
- D68 pad 1: /P23 -> /P22
- D68 pad 2: /P22 -> /P4
- D69 pad 1: /P23 -> /P22
- D69 pad 2: /P24 -> /P5
- D70 pad 1: /P11 -> /P22
- D70 pad 2: /P1 -> /P6
- D71 pad 1: /P11 -> /P22
- D71 pad 2: /P2 -> /P7
- D72 pad 1: /P11 -> /P22
- D72 pad 2: /P3 -> /P8
- D73 pad 1: /P11 -> /P22
- D73 pad 2: /P4 -> /P9
- D74 pad 1: /P11 -> /P22
- D74 pad 2: /P5 -> /P10
- D75 pad 1: /P11 -> /P22
- D75 pad 2: /P6 -> /P11
- D76 pad 1: /P11 -> /P22
- D76 pad 2: /P7 -> /P12
- D77 pad 1: /P11 -> /P22
- D77 pad 2: /P8 -> /P13
- D78 pad 1: /P11 -> /P22
- D78 pad 2: /P9 -> /P14
- D79 pad 1: /P11 -> /P22
- D79 pad 2: /P10 -> /P15
- D80 pad 1: /P11 -> /P22
- D80 pad 2: /P12 -> /P16
- D81 pad 1: /P11 -> /P22
- D81 pad 2: /P13 -> /P17
- D82 pad 1: /P11 -> /P22
- D82 pad 2: /P14 -> /P18
- D83 pad 1: /P11 -> /P22
- D83 pad 2: /P15 -> /P19
- D84 pad 1: /P11 -> /P22
- D84 pad 2: /P16 -> /P20
- D85 pad 1: /P11 -> /P22
- D85 pad 2: /P17 -> /P21
- D86 pad 1: /P11 -> /P22
- D86 pad 2: /P18 -> /P23
- D87 pad 1: /P11 -> /P22
- D87 pad 2: /P19 -> /P24
- D88 pad 1: /P11 -> /P6
- D88 pad 2: /P20 -> /P1
- D89 pad 1: /P11 -> /P6
- D89 pad 2: /P21 -> /P2
- D90 pad 1: /P11 -> /P6
- D90 pad 2: /P22 -> /P3
- D91 pad 1: /P11 -> /P6
- D91 pad 2: /P23 -> /P4
- D92 pad 1: /P11 -> /P6
- D92 pad 2: /P24 -> /P5
- D93 pad 1: /P22 -> /P6
- D93 pad 2: /P1 -> /P7
- D94 pad 1: /P22 -> /P6
- D94 pad 2: /P2 -> /P8
- D95 pad 1: /P22 -> /P6
- D95 pad 2: /P3 -> /P9
- D96 pad 1: /P22 -> /P6
- D96 pad 2: /P4 -> /P10
- D97 pad 1: /P22 -> /P21
- D97 pad 2: /P5 -> /P1
- D98 pad 1: /P22 -> /P21
- D98 pad 2: /P6 -> /P2
- D99 pad 1: /P22 -> /P21
- D99 pad 2: /P7 -> /P3
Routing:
- net /P13: track 431.0 -> 68.8 mm, vias 89 -> 23
- net /P20: track 377.2 -> 45.8 mm, vias 89 -> 15
- net /P21: track 375.9 -> 45.8 mm, vias 89 -> 15
- net /P22: track 374.6 -> 45.8 mm, vias 89 -> 15
- net /P23: track 372.0 -> 45.8 mm, vias 89 -> 15
- net /P14: track 386.3 -> 68.8 mm, vias 89 -> 23
- net /P15: track 385.1 -> 68.8 mm, vias 89 -> 23
- net /P16: track 382.9 -> 68.8 mm, vias 89 -> 23
- net /P17: track 381.4 -> 68.8 mm, vias 89 -> 23
- net /P18: track 380.0 -> 68.8 mm, vias 89 -> 23
- net /P19: track 378.6 -> 68.8 mm, vias 89 -> 23
- net /P6: track 362.0 -> 65.8 mm, vias 89 -> 23
- net /P7: track 363.8 -> 68.8 mm, vias 89 -> 23
- net /P5: track 361.1 -> 68.8 mm, vias 89 -> 23
- net /P8: track 362.6 -> 70.9 mm, vias 89 -> 23
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
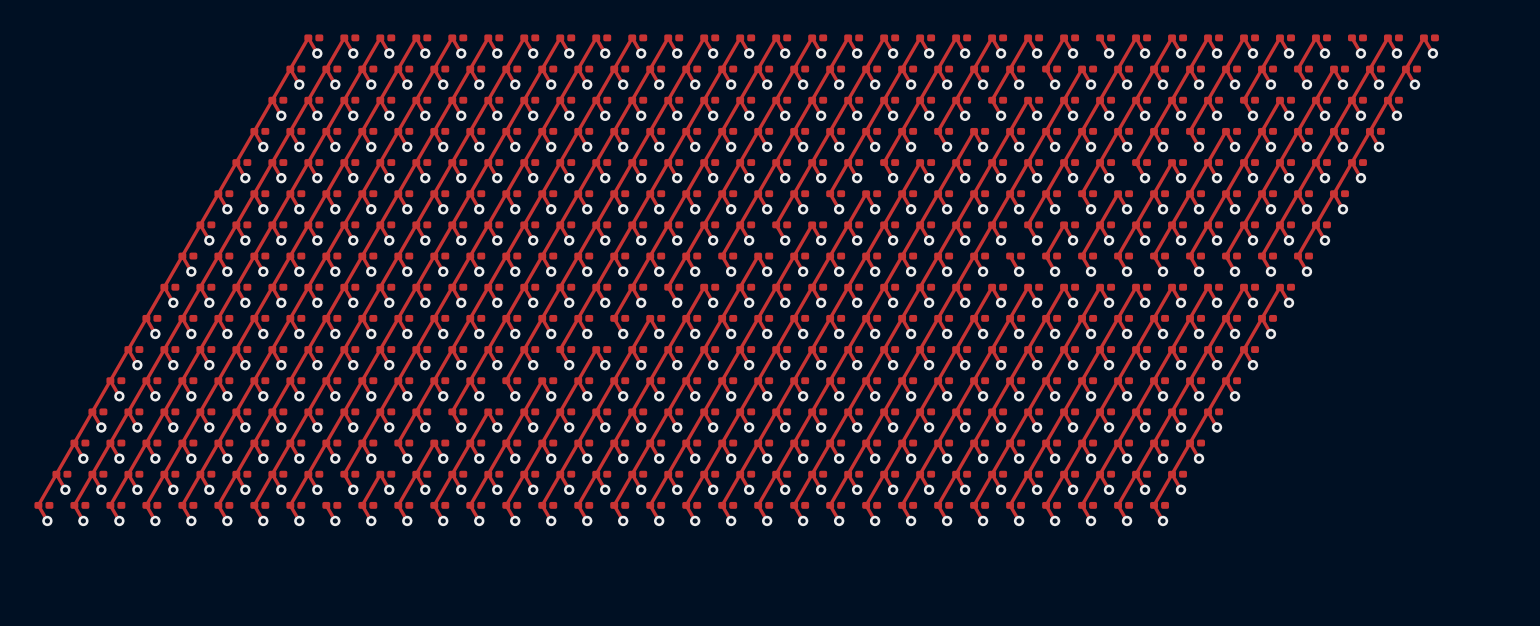
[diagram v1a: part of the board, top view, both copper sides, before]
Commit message: Fix via wiring and add horizontal tracks to back. Also stitch some front nets together.
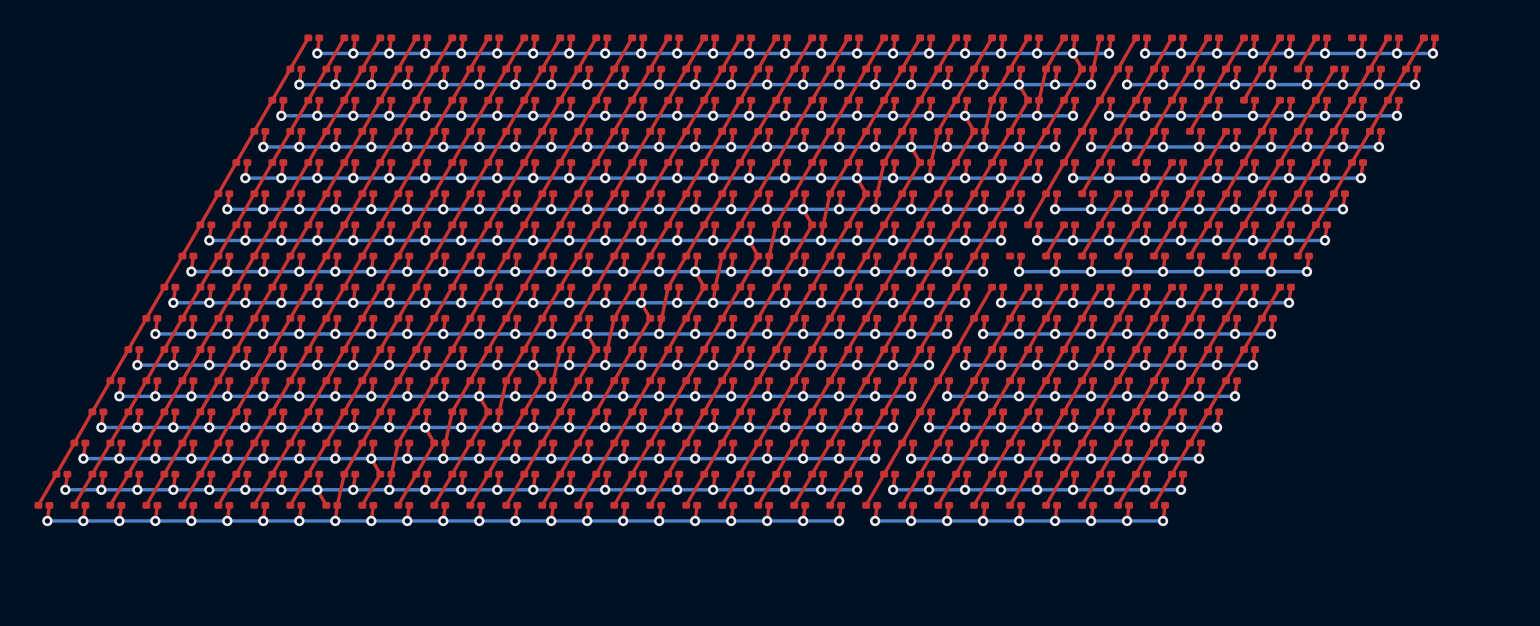
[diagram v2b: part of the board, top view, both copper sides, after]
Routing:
- net /P21: track 45.8 -> 100.0 mm, vias 15 -> 23
- net /P22: track 45.8 -> 100.0 mm, vias 15 -> 23
- net /P20: track 45.8 -> 100.0 mm, vias 15 -> 23
- net /P23: track 45.8 -> 100.0 mm, vias 15 -> 23
- net /P24: track 47.9 -> 100.3 mm, vias 15 -> 23
- net /P15: track 68.8 -> 115.0 mm
- net /P13: track 68.8 -> 114.7 mm
- net /P12: track 68.8 -> 114.7 mm
- net /P10: track 68.8 -> 114.7 mm
- net /P19: track 68.8 -> 114.7 mm
- net /P14: track 68.8 -> 114.7 mm
- net /P18: track 68.8 -> 114.7 mm
- net /P17: track 68.8 -> 114.7 mm
- net /P11: track 68.8 -> 114.7 mm
- net /P16: track 68.8 -> 114.7 mm
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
